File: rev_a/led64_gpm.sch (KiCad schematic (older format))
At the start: 24 parts, among them J1 MB_TERMINATE, U1 MAX3051ESA, U2 L78L33AC, U3 LPC175X, X1 20MHZ

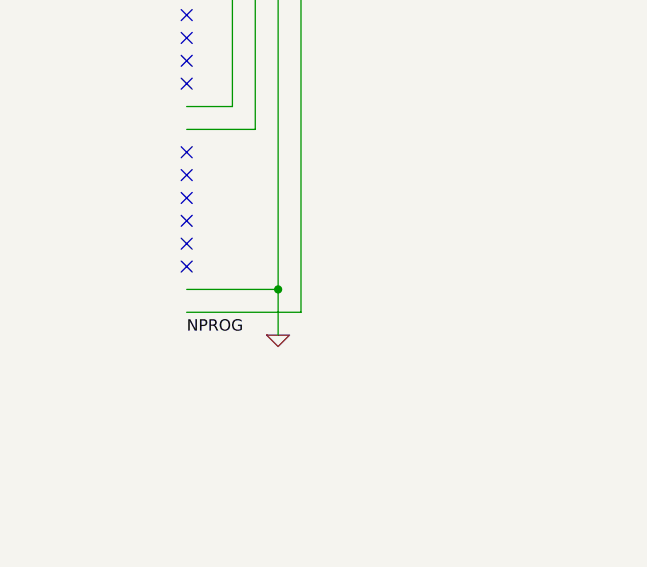
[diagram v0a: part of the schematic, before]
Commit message: renamed files. Now supports a simple LED and resistor in series
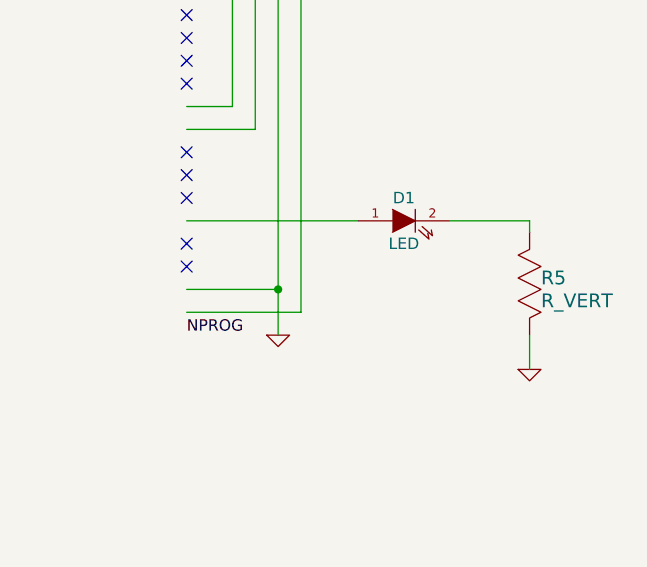
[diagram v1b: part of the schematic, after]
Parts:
- added D1: LED, ~, symbol LED
- added R5: R_VERT, symbol R_VERT
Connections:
- wire segments 112 -> 116
- no-connect marks 52 -> 51
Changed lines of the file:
@@
-EESchema Schematic File Version 2
+EESchema Schematic File Version 2  date Saturday, July 13, 2013 12:04:53 PM
 LIBS:power
 LIBS:device
@@
 LIBS:lpc175x_template
 LIBS:lpc175x_template-cache
-EELAYER 24 0
+EELAYER 27 0
 EELAYER END
 $Descr A4 11693 8268
@@
 Sheet 1 1
 Title ""
-Date "19 jul 2012"
+Date "13 jul 2013"
 Rev ""
 Comp ""
@@
 $EndComp
 $Comp
-L +3.3V #PWR01
+L +3.3V #PWR7
 U 1 1 4FFF2D21
 P 2100 6100
-F 0 "#PWR01" H 2100 6060 30  0001 C CNN
+F 0 "#PWR7" H 2100 6060 30  0001 C CNN
 F 1 "+3.3V" H 2100 6220 50  0000 C CNN
 F 2 "" H 2100 6100 60  0001 C CNN
@@
 FILTER CAPACITORS
 $Comp
-L GND #PWR02
+L GND #PWR4
 U 1 1 4FFE6188
 P 1600 1700
-F 0 "#PWR02" H 1600 1700 30  0001 C CNN
+F 0 "#PWR4" H 1600 1700 30  0001 C CNN
 F 1 "GND" H 1600 1630 30  0001 C CNN
 F 2 "" H 1600 1700 60  0001 C CNN
@@
 $EndComp
 $Comp
-L +3.3V #PWR03
+L +3.3V #PWR3
 U 1 1 4FFE6183
 P 1600 900
-F 0 "#PWR03" H 1600 860 30  0001 C CNN
+F 0 "#PWR3" H 1600 860 30  0001 C CNN
 F 1 "+3.3V" H 1600 1020 50  0000 C CNN
 F 2 "" H 1600 900 60  0001 C CNN
@@
 NoConn ~ 6700 4400
 NoConn ~ 6700 4500
-NoConn ~ 6700 4600
 NoConn ~ 6700 4700
 NoConn ~ 6700 4800
@@
 NoConn ~ 3500 1700
 $Comp
-L GND #PWR04
+L GND #PWR10
 U 1 1 4FFE2185
 P 2800 3700
-F 0 "#PWR04" H 2800 3700 30  0001 C CNN
+F 0 "#PWR10" H 2800 3700 30  0001 C CNN
 F 1 "GND" H 2800 3630 30  0001 C CNN
 F 2 "" H 2800 3700 60  0001 C CNN
@@
 TXD
 $Comp
-L +3.3V #PWR05
+L +3.3V #PWR15
 U 1 1 4FFE1D6D
 P 7200 1300
-F 0 "#PWR05" H 7200 1260 30  0001 C CNN
+F 0 "#PWR15" H 7200 1260 30  0001 C CNN
 F 1 "+3.3V" H 7200 1420 50  0000 C CNN
 F 2 "" H 7200 1300 60  0001 C CNN
@@
 $EndComp
 $Comp
-L +3.3V #PWR06
+L +3.3V #PWR11
 U 1 1 4FFE1D13
 P 3100 1800
-F 0 "#PWR06" H 3100 1760 30  0001 C CNN
+F 0 "#PWR11" H 3100 1760 30  0001 C CNN
 F 1 "+3.3V" H 3100 1920 50  0000 C CNN
 F 2 "" H 3100 1800 60  0001 C CNN
@@
 $EndComp
 $Comp
-L GND #PWR07
+L GND #PWR12
 U 1 1 4FFE1CB6
 P 3200 4600
-F 0 "#PWR07" H 3200 4600 30  0001 C CNN
+F 0 "#PWR12" H 3200 4600 30  0001 C CNN
 F 1 "GND" H 3200 4530 30  0001 C CNN
 F 2 "" H 3200 4600 60  0001 C CNN
@@
 $EndComp
 $Comp
-L GND #PWR08
+L GND #PWR14
 U 1 1 4FFE1C7D
 P 7100 5100
-F 0 "#PWR08" H 7100 5100 30  0001 C CNN
+F 0 "#PWR14" H 7100 5100 30  0001 C CNN
 F 1 "GND" H 7100 5030 30  0001 C CNN
 F 2 "" H 7100 5100 60  0001 C CNN
@@
 TDO
 $Comp
-L GND #PWR09
+L GND #PWR1
 U 1 1 4FFE0F4E
 P 1400 4500
-F 0 "#PWR09" H 1400 4500 30  0001 C CNN
+F 0 "#PWR1" H 1400 4500 30  0001 C CNN
 F 1 "GND" H 1400 4430 30  0001 C CNN
 F 2 "" H 1400 4500 60  0001 C CNN
@@
 NoConn ~ 1200 3900
 $Comp
-L GND #PWR010
+L GND #PWR2
 U 1 1 4FFA0CB2
 P 1400 6500
-F 0 "#PWR010" H 1400 6500 30  0001 C CNN
+F 0 "#PWR2" H 1400 6500 30  0001 C CNN
 F 1 "GND" H 1400 6430 30  0001 C CNN
 F 2 "" H 1400 6500 60  0001 C CNN
@@
 $EndComp
 $Comp
-L +3.3V #PWR011
+L +3.3V #PWR5
 U 1 1 4FF7A675
 P 2000 4300
-F 0 "#PWR011" H 2000 4260 30  0001 C CNN
+F 0 "#PWR5" H 2000 4260 30  0001 C CNN
 F 1 "+3.3V" H 2000 4420 50  0000 C CNN
 F 2 "" H 2000 4300 60  0001 C CNN
@@
 $EndComp
 $Comp
-L GND #PWR012
+L GND #PWR13
 U 1 1 4FF78458
 P 3300 7200
-F 0 "#PWR012" H 3300 7200 30  0001 C CNN
+F 0 "#PWR13" H 3300 7200 30  0001 C CNN
 F 1 "GND" H 3300 7130 30  0001 C CNN
 F 2 "" H 3300 7200 60  0001 C CNN
@@
 $EndComp
 $Comp
-L GND #PWR013
+L GND #PWR8
 U 1 1 4FF7842B
 P 2100 6600
-F 0 "#PWR013" H 2100 6600 30  0001 C CNN
+F 0 "#PWR8" H 2100 6600 30  0001 C CNN
 F 1 "GND" H 2100 6530 30  0001 C CNN
 F 2 "" H 2100 6600 60  0001 C CNN
@@
 $EndComp
 $Comp
-L +3.3V #PWR014
+L +3.3V #PWR9
 U 1 1 4FF78172
 P 2600 6800
-F 0 "#PWR014" H 2600 6760 30  0001 C CNN
+F 0 "#PWR9" H 2600 6760 30  0001 C CNN
 F 1 "+3.3V" H 2600 6920 50  0000 C CNN
 F 2 "" H 2600 6800 60  0001 C CNN
@@
 $EndComp
 $Comp
-L GND #PWR015
+L GND #PWR6
 U 1 1 4FF78111
 P 2050 7600
-F 0 "#PWR015" H 2050 7600 30  0001 C CNN
+F 0 "#PWR6" H 2050 7600 30  0001 C CNN
 F 1 "GND" H 2050 7530 30  0001 C CNN
 F 2 "" H 2050 7600 60  0001 C CNN
@@
 	3500 3100 2800 3100
 Connection ~ 2800 3100
+$Comp
+L LED D1
+U 1 1 51E1A603
+P 7650 4600
+F 0 "D1" H 7650 4700 50  0000 C CNN
+F 1 "LED" H 7650 4500 50  0000 C CNN
+F 2 "~" H 7650 4600 60  0000 C CNN
+F 3 "~" H 7650 4600 60  0000 C CNN
+	1    7650 4600
+	1    0    0    -1
+$EndComp
+$Comp
+L R_VERT R5
+U 1 1 51E1A612
+P 8200 4850
+F 0 "R5" H 8250 4850 60  0000 L CNN
+F 1 "R_VERT" H 8250 4750 60  0000 L CNN
+F 2 "" H 8200 4850 60  0000 C CNN
+F 3 "" H 8200 4850 60  0000 C CNN
+	1    8200 4850
+	1    0    0    -1
+$EndComp
+Wire Wire Line
+	6700 4600 7450 4600
+Wire Wire Line
+	7850 4600 8200 4600
+Wire Wire Line
+	8200 4600 8200 4650
+$Comp
+L GND #PWR16
+U 1 1 51E1A746
+P 8200 5250
+F 0 "#PWR16" H 8200 5250 30  0001 C CNN
+F 1 "GND" H 8200 5180 30  0001 C CNN
+F 2 "" H 8200 5250 60  0000 C CNN
+F 3 "" H 8200 5250 60  0000 C CNN
+	1    8200 5250
+	1    0    0    -1
+$EndComp
+Wire Wire Line
+	8200 5100 8200 5250
 $EndSCHEMATC
